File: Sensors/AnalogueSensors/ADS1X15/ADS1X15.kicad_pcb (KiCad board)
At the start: 2 copper layers, 17.5 x 22.6 mm, 20 parts, among them J1 Conn_01x05, J2 Conn_01x05

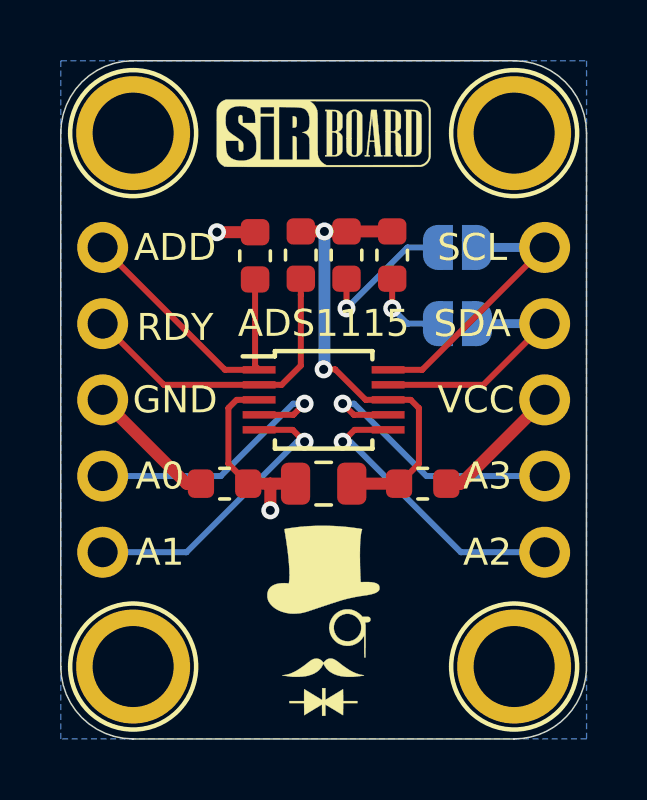
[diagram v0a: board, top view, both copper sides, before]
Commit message: ADS1X15 Added in place of ADS1015 and ADS1115
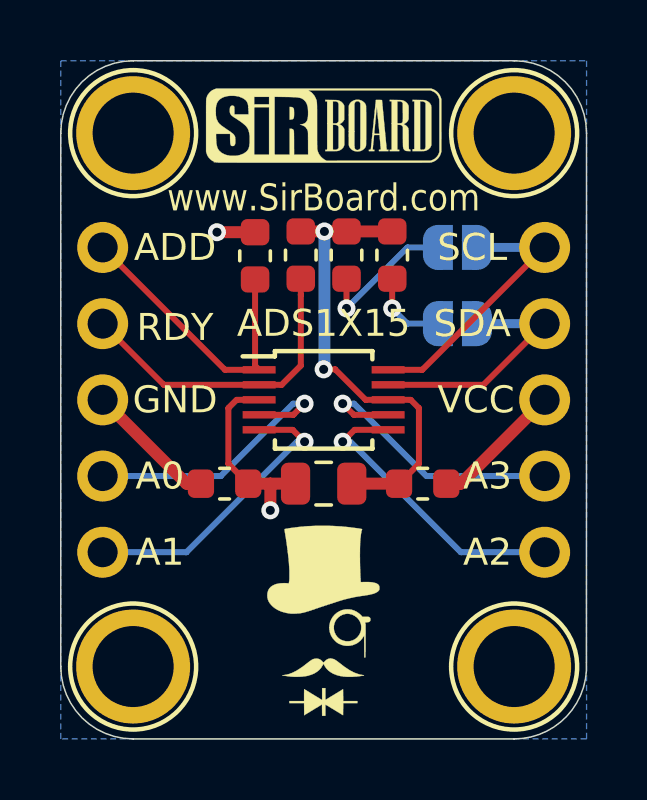
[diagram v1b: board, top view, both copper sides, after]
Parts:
- G***: footprint logo:SirBoard71X22 -> logo:SirBoard79x25
- moved G*** 0.25 mm to (65.5, 29.3)
- renumbered ADS1115 to ADS1X15, SCL1 to SCL, SDA1 to SDA
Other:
- board text added: "12 Bit 16 Bit"
- board text added: "ADS1X15"
- board text added: "www.SirBoard.com"
- board text removed: "ADS1115 4 Channel 16 Bit ADC"
